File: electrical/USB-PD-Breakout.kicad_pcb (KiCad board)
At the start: 2 copper layers, 34.5 x 28 mm, 25 parts, among them J1 USB-C_Female, J2 USB_OTG, J3 CONN_02X03, J4 Conn_01x08_Male, U1 FUSB302BMPX, X1 MTHOLE, X2 MTHOLE

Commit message: Mod: Project so it could be easy ordered over JLCPCB
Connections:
- net /~INT renamed /~{INT}
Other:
- net class Default removed

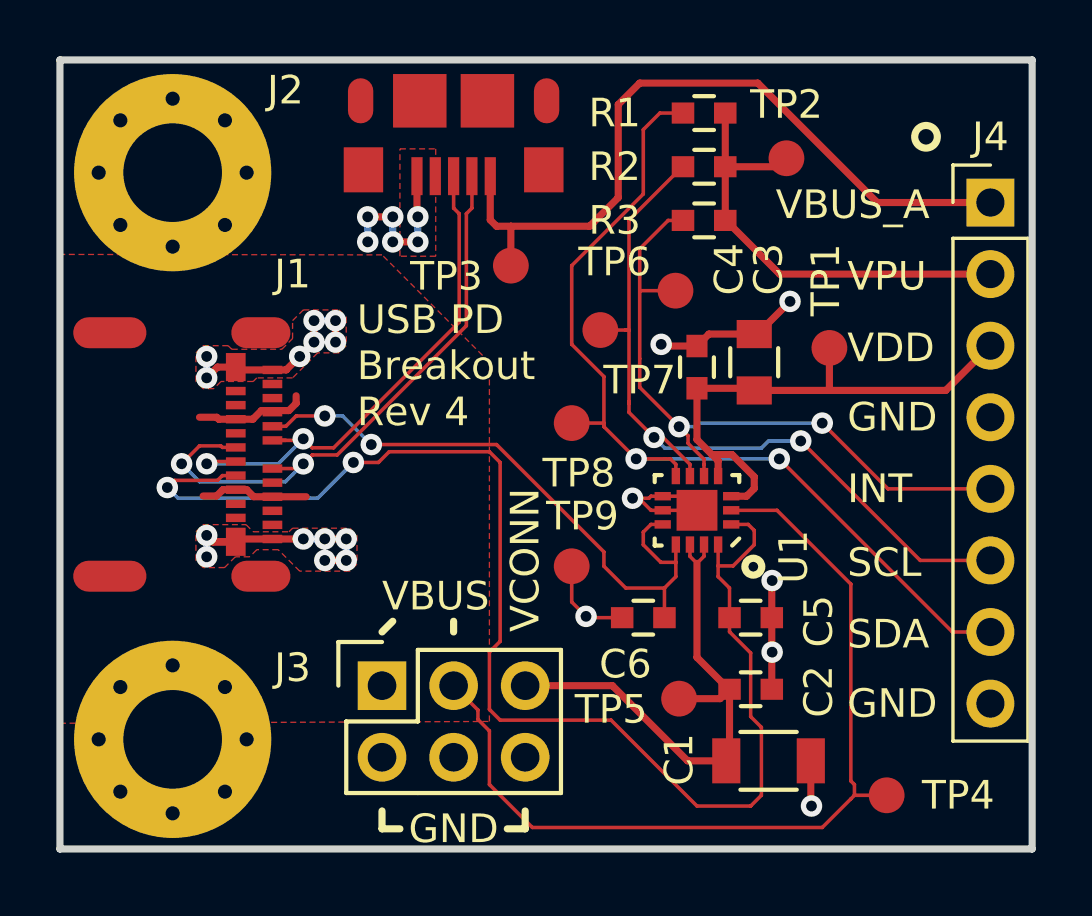
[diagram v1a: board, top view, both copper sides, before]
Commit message: Bug: Fixed the non existing holes in the USB footprints Mod: Changed the planes (GND and VBUS) from thermal relief to solid
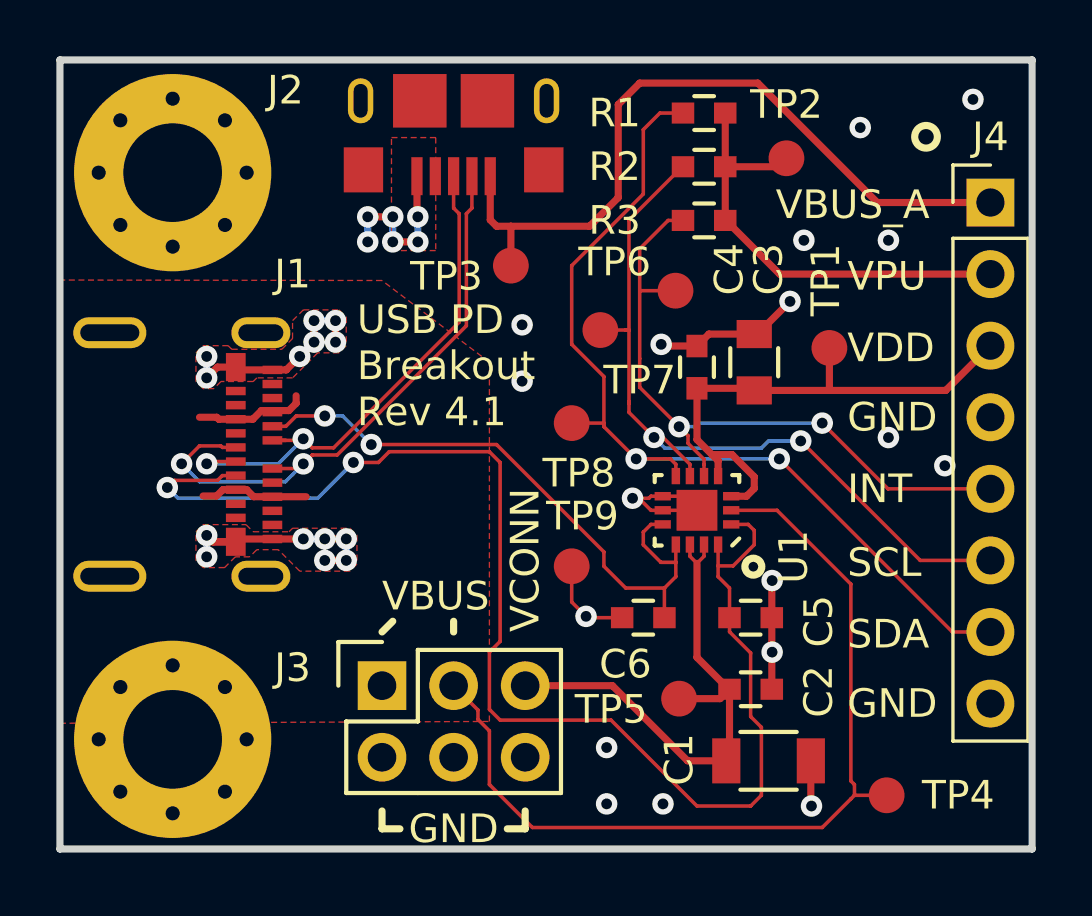
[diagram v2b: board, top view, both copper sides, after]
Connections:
- J1 pad SHLD: Net-(J1-PadSHLD) -> GND
- J2 pad 10: (no net) -> GND
- J2 pad 6: Net-(J2-Pad6) -> GND
- J2 pad 7: (no net) -> GND
- J2 pad 8: (no net) -> GND
- J2 pad 9: (no net) -> GND
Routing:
- net GND: vias 27 -> 38
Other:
- board text added: "USB PD Breakout Rev 4.1"
- board text added: "USB PowerDelivery Breakout Board Rev 4.1 ReclaimerLabs.com feat. ElektronNik Zoller"
- board text removed: "USB PD Breakout Rev 4"
- board text removed: "USB PowerDelivery Breakout Board Rev 4 ReclaimerLabs.com"
